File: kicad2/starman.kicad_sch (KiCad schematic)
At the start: 183 parts, among them J1 Conn_01x12, J2 Conn_01x10, J3 Conn_01x12, U1 ESP32-S2-MINI-1, U2 PCA9959, U3 PCA9959, U4 PCA9959, U5 PCA9959, U6 PCA9959, U7 PCA9959, U8 MIC29310-5.0WU, U9 LF33_TO220, Y1 20Mhz, Y2 20Mhz, Y3 20Mhz, Y4 20Mhz, Y5 20Mhz, Y6 20Mhz

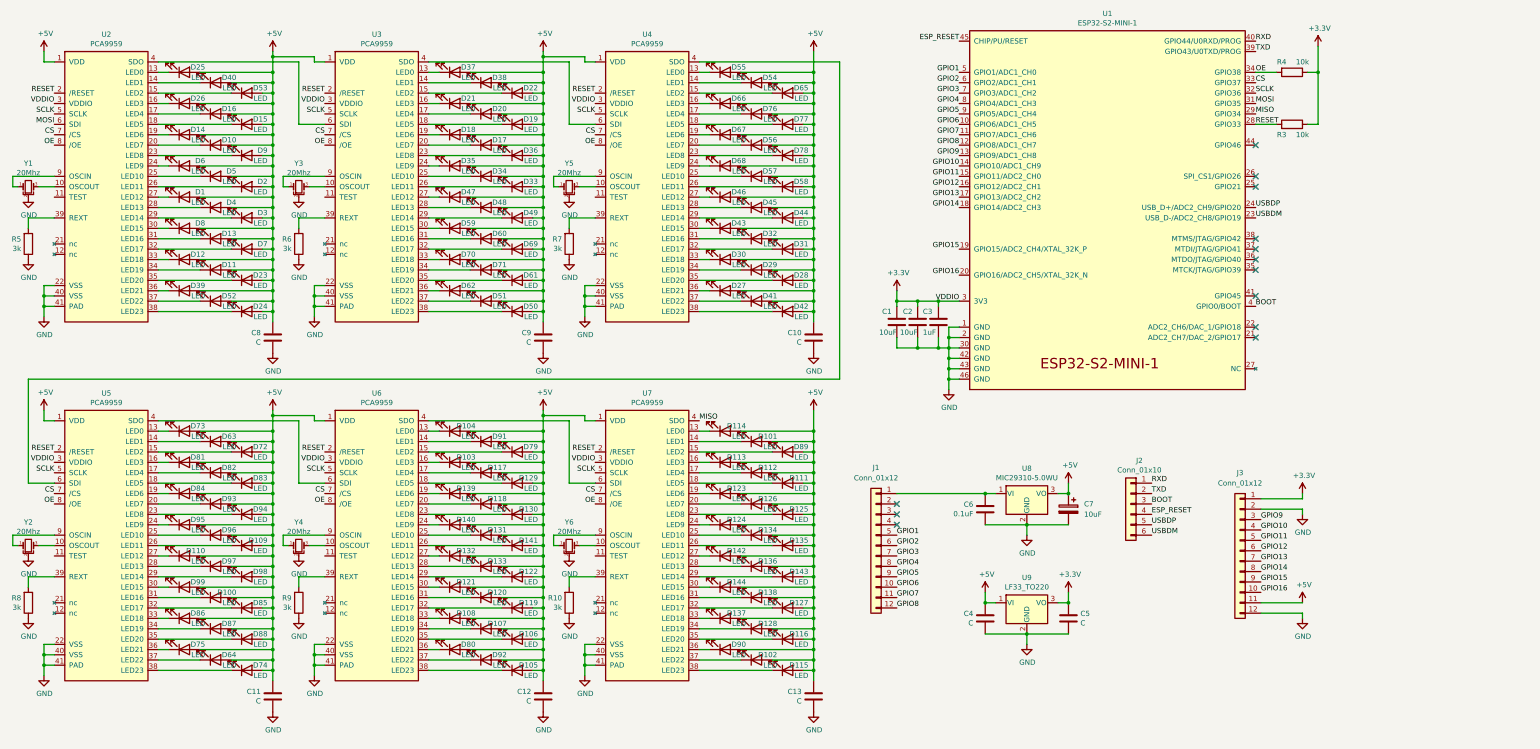
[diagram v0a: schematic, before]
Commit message: Complete routing of all GPIO pins
Also fixed paths to 3d components
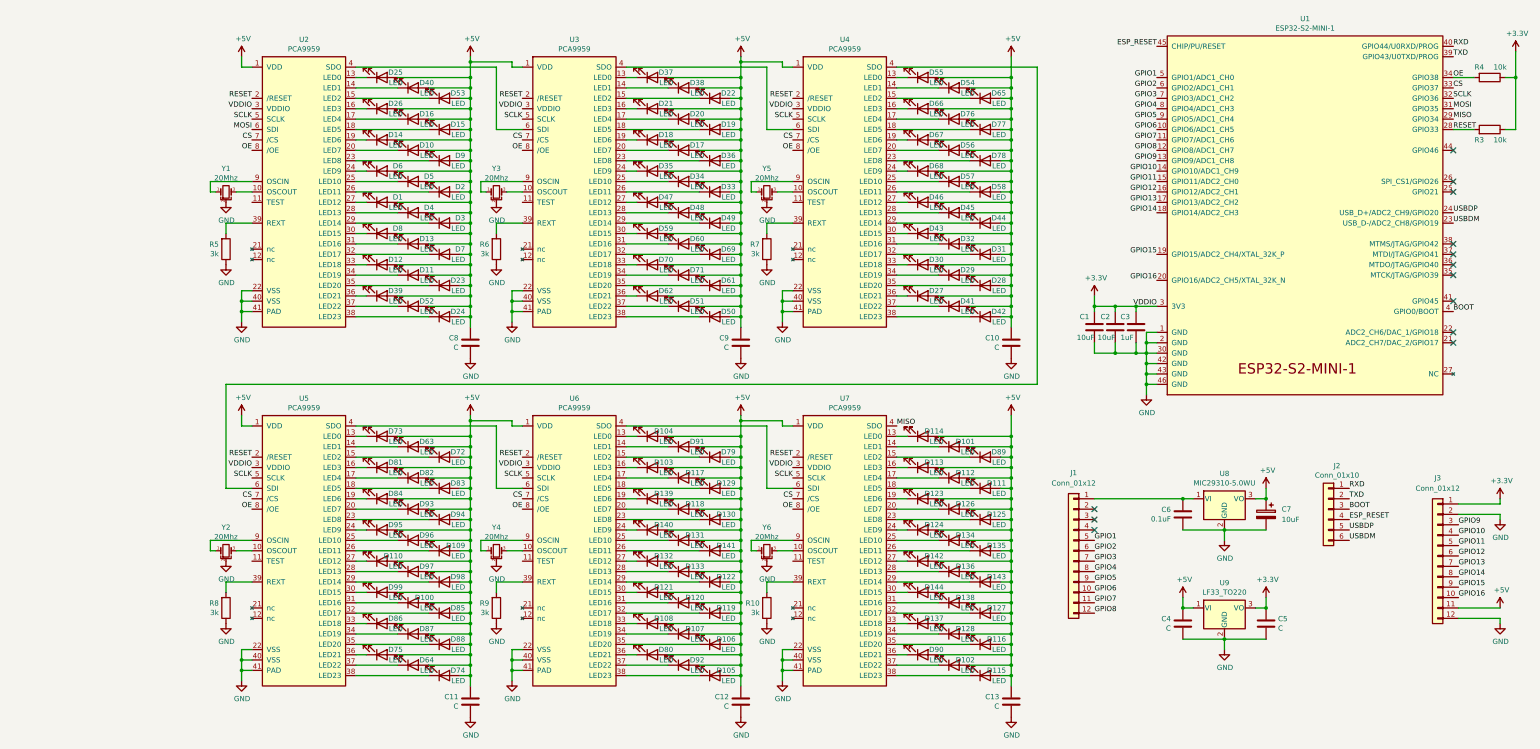
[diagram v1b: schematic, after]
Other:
- moved on the sheet: C1, C10, C11, C12, C13, C2, C3, C4, C5, C6, C7, C8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

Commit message: Added daughter board for power and buttons
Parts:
- added C14: 0.1uF, Capacitor_SMD:C_0805_2012Metric, symbol Device:C
- added C15: (no value), Capacitor_SMD:C_0805_2012Metric, symbol Device:C
- added J10: Barrel_Jack_MountingPin, Connector_BarrelJack:BarrelJack_CUI_PJ-063AH_Horizontal, symbol Connector:Barrel_Jack_MountingPin
- added J11: USB_B_Micro, Connector_USB:USB_Micro-B_Molex-105133-0031, symbol Connector:USB_B_Micro
- added J4: Conn_01x10, Connector_PinHeader_2.54mm:PinHeader_1x06_P2.54mm_Vertical, symbol Connector_Generic:Conn_01x06
- added J5: Conn_02x03_Counter_Clockwise, Connector_PinHeader_2.54mm:PinHeader_2x03_P2.54mm_Vertical, symbol Connector_Generic:Conn_02x03_Counter_Clockwise
- added J6, J8: Conn_01x12, Connector_PinHeader_2.54mm:PinHeader_1x12_P2.54mm_Vertical, symbol Connector_Generic:Conn_01x12
- added J7: Conn_01x10, Connector_PinHeader_2.54mm:PinHeader_1x10_P2.54mm_Vertical, symbol Connector_Generic:Conn_01x10
- added J9: Conn_01x08, Connector_PinHeader_2.54mm:PinHeader_1x10_P2.54mm_Vertical, symbol Connector_Generic:Conn_01x10
- added R1, R3: 10k, Resistor_SMD:R_0805_2012Metric, symbol Device:R
- added R2: (no value), Resistor_SMD:R_0805_2012Metric, symbol Device:R
- added SW1, SW2: (no value), symbol Switch:SW_SPST
- added SW3: SW_SPST, Button_Switch_SMD:SW_SPST_PTS810, symbol Switch:SW_SPST
- renumbered R4 to R11, R3 to R12
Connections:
- net BOOT renamed GPIO0
- net ESP_RESET renamed EN
- new net +3.3VA: J7.1 (Pin_1), J8.1 (Pin_1), R1.2, R2.2, R3.2
- new net +5VA: J8.11 (Pin_11), J9.1 (Pin_1)
- new net GNDA: C14.1, C15.1, J10.2, J10.MP (MountPin), J11.5 (GND), J11.6 (Shield), J5.2 (Pin_2), J7.10 (Pin_10), J8.12 (Pin_12), J8.2 (Pin_2), J9.10 (Pin_10), SW1.2 (B), SW2.2 (B), SW3.2 (B)
- new net VCC: J10.1, J6.1 (Pin_1)
- new net ext_EN: C14.2, C15.2, J4.4 (Pin_4), J5.4 (Pin_4), R2.1, SW2.1 (A)
- new net ext_GPIO0: J4.3 (Pin_3), J5.1 (Pin_1), R1.1, SW1.1 (A)
- new net ext_GPIO1: J6.5 (Pin_5), J7.2 (Pin_2), R3.1, SW3.1 (A)
- new net ext_GPIO10: J8.4 (Pin_4), J9.3 (Pin_3)
- new net ext_GPIO11: J8.5 (Pin_5), J9.4 (Pin_4)
- new net ext_GPIO12: J8.6 (Pin_6), J9.5 (Pin_5)
- new net ext_GPIO13: J8.7 (Pin_7), J9.6 (Pin_6)
- new net ext_GPIO14: J8.8 (Pin_8), J9.7 (Pin_7)
- new net ext_GPIO15: J8.9 (Pin_9), J9.8 (Pin_8)
- new net ext_GPIO16: J8.10 (Pin_10), J9.9 (Pin_9)
- new net ext_GPIO2: J6.6 (Pin_6), J7.3 (Pin_3)
- new net ext_GPIO3: J6.7 (Pin_7), J7.4 (Pin_4)
- new net ext_GPIO4: J6.8 (Pin_8), J7.5 (Pin_5)
- new net ext_GPIO5: J6.9 (Pin_9), J7.6 (Pin_6)
- new net ext_GPIO6: J6.10 (Pin_10), J7.7 (Pin_7)
- new net ext_GPIO7: J6.11 (Pin_11), J7.8 (Pin_8)
- new net ext_GPIO8: J6.12 (Pin_12), J7.9 (Pin_9)
- new net ext_GPIO9: J8.3 (Pin_3), J9.2 (Pin_2)
- new net ext_RXD: J4.1 (Pin_1), J5.6 (Pin_6)
- new net ext_TXD: J4.2 (Pin_2), J5.5 (Pin_5)
- new net ext_USBDM: J11.2 (D-), J4.6 (Pin_6)
- new net ext_USBDP: J11.3 (D+), J4.5 (Pin_5)
- no-connect marks 13 -> 19

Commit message: Added sound resistors, channels, volume, and speaker
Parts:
- removed J11: USB_B_Micro, Connector_USB:USB_Micro-B_Molex-105133-0031, symbol Connector:USB_B_Micro
- removed R1: 10k, Resistor_SMD:R_0805_2012Metric, symbol Device:R
- removed SW1: (no value), symbol Switch:SW_SPST
- added LS1: (no value), symbol Device:Speaker
- added R4, R5, R6: 75, Resistor_SMD:R_0805_2012Metric, symbol Device:R
- added R7: (no value), Resistor_SMD:R_0805_2012Metric, symbol Device:R
- added RV1: (no value), symbol Device:R_Potentiometer
- C15: value (none) -> 1uF
- J4: value Conn_01x10 -> (none); footprint Connector_PinHeader_2.54mm:PinHeader_1x06_P2.54mm_Vertical -> (none)
- R2: value (none) -> 10k
- SW1: renamed from SW2; value (none) -> SW_SPST; footprint (none) -> Button_Switch_SMD:SW_SPST_PTS810
- renumbered R7 to R10, R8 to R11, R9 to R12, R10 to R13, R11 to R14, R12 to R15, R5 to R8, R6 to R9, SW3 to SW2
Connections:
- net ext_USBDM is gone; now on net GNDA: J4.6 (Pin_6)
- net GND: now also J2.6 (Pin_6)
- net GNDA: now also LS1.2
- net at U1.21 (ADC2_CH7/DAC_2/GPIO17): now also R4.2
- net at U1.22 (ADC2_CH6/DAC_1/GPIO18): now also R5.2
- net USBDM: no longer names the net of U1.23 (USB_D-/ADC2_CH8/GPIO19)
- net USBDM: now also R6.2; no longer J2.6 (Pin_6)
- net USBDP: no longer names the net of U1.24 (USB_D+/ADC2_CH9/GPIO20)
- net USBDP: now also R7.2; no longer J2.5 (Pin_5)
- net ext_USBDP renamed ext_SOUND
- net ext_SOUND: now also RV1.1
- new net: LS1.1, RV1.3
- new net SOUND: J2.5 (Pin_5), R4.1, R5.1, R6.1, R7.1
- no-connect marks 19 -> 16
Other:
- moved on the sheet: C14, C15, J10, J4, J5, R2, R3, SW1, SW2

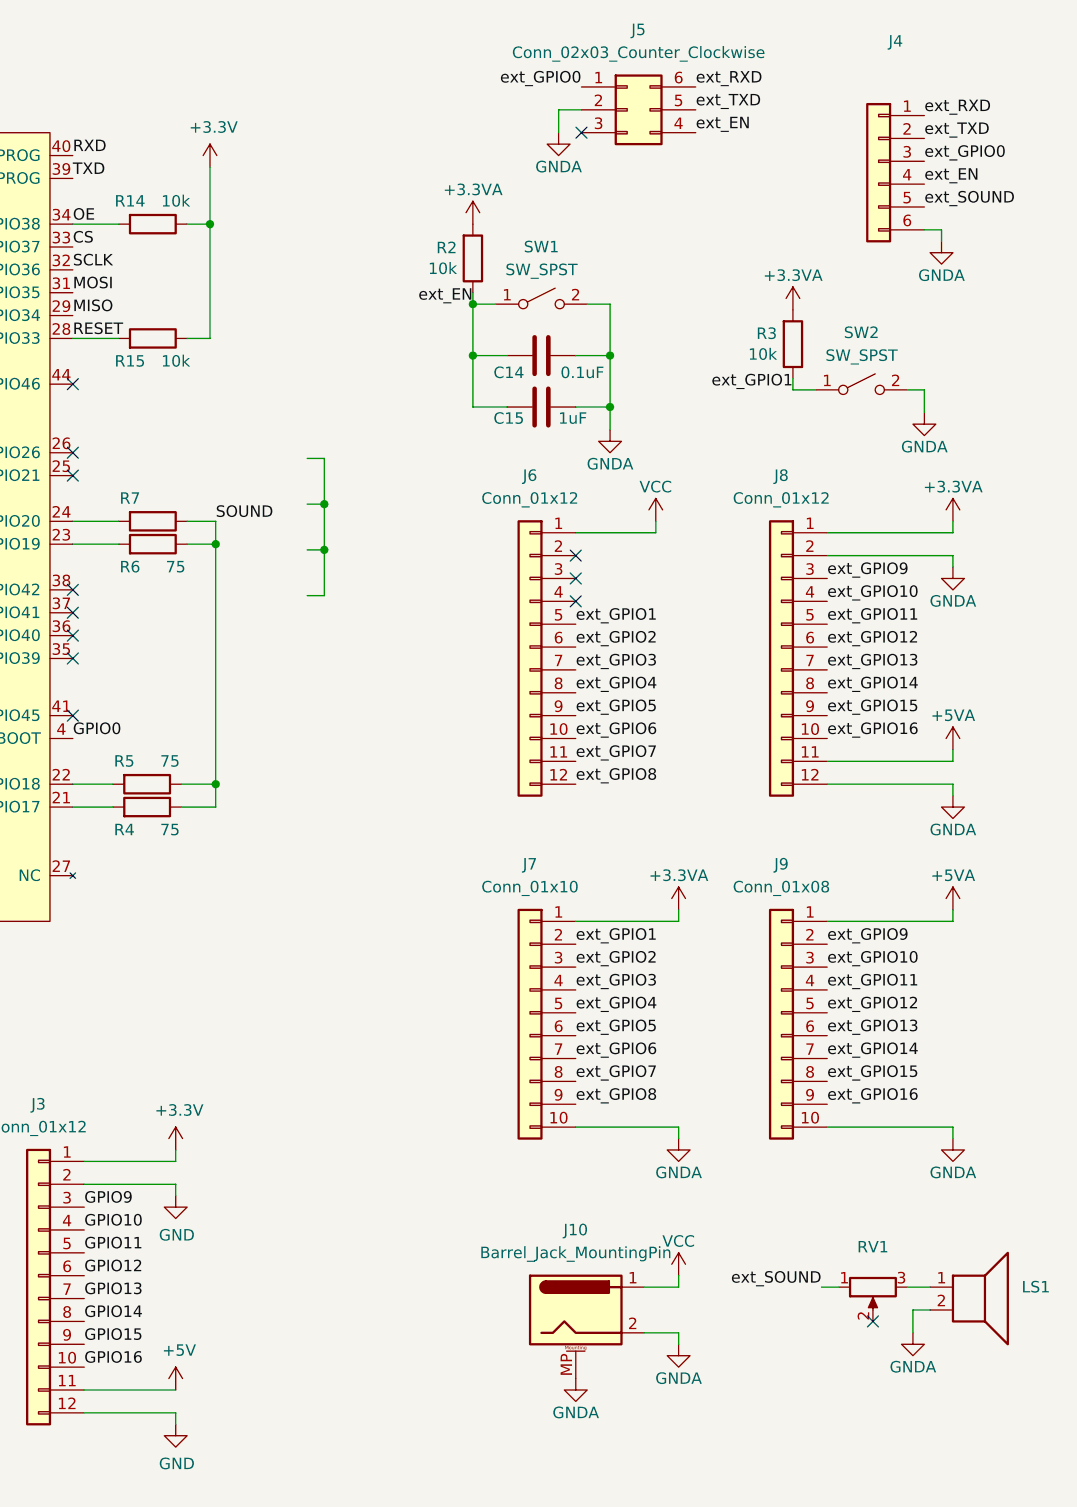
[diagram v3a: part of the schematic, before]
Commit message: Fixed DRC errors
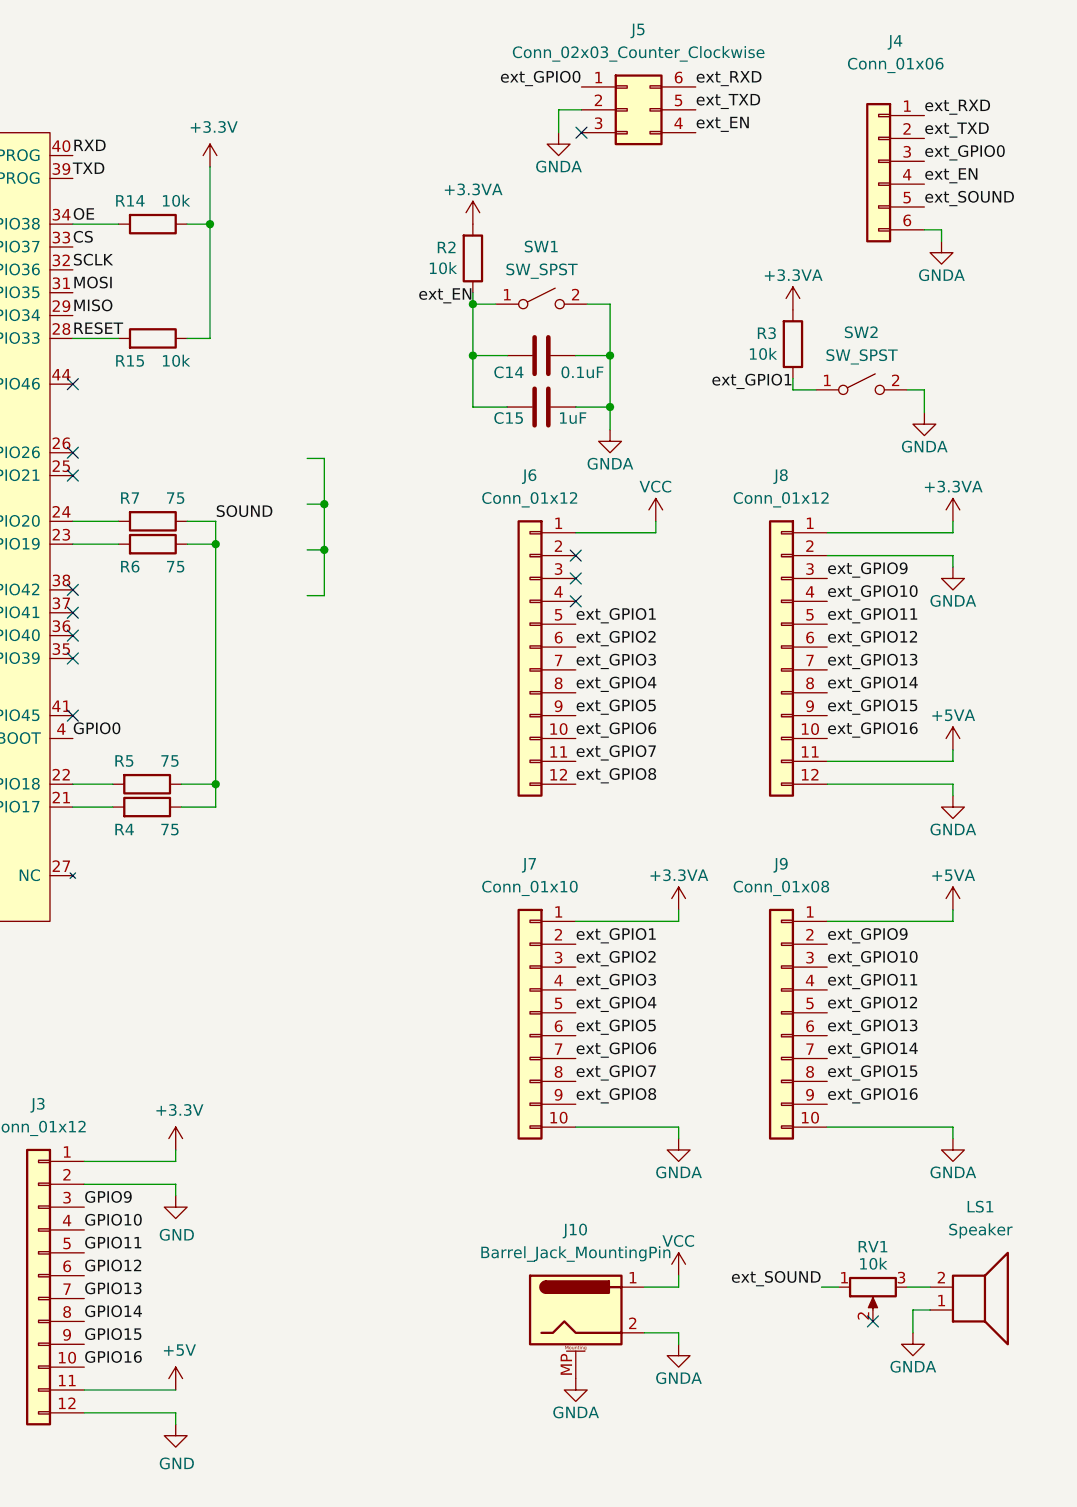
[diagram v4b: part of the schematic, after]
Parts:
- J4: value (none) -> Conn_01x06; footprint (none) -> Connector_PinHeader_2.54mm:PinHeader_1x06_P2.54mm_Vertical
- LS1: value (none) -> Speaker; footprint (none) -> Buzzer_Beeper:MagneticBuzzer_StarMicronics_HMB-06_HMB-12
- R7: value (none) -> 75
- RV1: value (none) -> 10k; footprint (none) -> Potentiometer_SMD:Potentiometer_ACP_CA9-VSMD_Vertical
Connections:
- net GNDA: now also LS1.1; no longer LS1.2
- net at RV1.3: now also LS1.2; no longer LS1.1
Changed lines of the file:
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@@
     (in_bom yes) (on_board yes)
     (property "Reference" "J4" (id 0) (at 410.21 10.16 0))
-    (property "Value" "" (id 1) (at 410.21 12.7 0))
-    (property "Footprint" "" (id 2) (at 408.305 23.495 0)
+    (property "Value" "Conn_01x06" (id 1) (at 410.21 12.7 0))
+    (property "Footprint" "Connector_PinHeader_2.54mm:PinHeader_1x06_P2.54mm_Vertical" (id 2) (at 408.305 23.495 0)
       (effects (font (size 1.27 1.27)) hide)
     )
@@
     (pin "1")
   )
-  (symbol (lib_id "Device:Speaker") (at 419.1 148.59 0) (unit 1)
+  (symbol (lib_id "Device:Speaker") (at 419.1 151.13 0) (mirror x) (unit 1)
     (in_bom yes) (on_board yes) (fields_autoplaced)
-    (property "Reference" "LS1" (id 0) (at 424.18 148.5899 0)
-      (effects (font (size 1.27 1.27)) (justify left))
-    )
-    (property "Value" "" (id 1) (at 424.18 151.1299 0)
-      (effects (font (size 1.27 1.27)) (justify left))
-    )
-    (property "Footprint" "" (id 2) (at 419.1 153.67 0)
+    (property "Reference" "LS1" (id 0) (at 419.608 139.7 0))
+    (property "Value" "Speaker" (id 1) (at 419.608 142.24 0))
+    (property "Footprint" "Buzzer_Beeper:MagneticBuzzer_StarMicronics_HMB-06_HMB-12" (id 2) (at 419.1 146.05 0)
       (effects (font (size 1.27 1.27)) hide)
     )
@@
     (in_bom yes) (on_board yes)
     (property "Reference" "RV1" (id 0) (at 407.67 144.145 90))
-    (property "Value" "" (id 1) (at 407.67 146.05 90))
-    (property "Footprint" "" (id 2) (at 407.67 148.59 0)
+    (property "Value" "10k" (id 1) (at 407.67 146.05 90))
+    (property "Footprint" "Potentiometer_SMD:Potentiometer_ACP_CA9-VSMD_Vertical" (id 2) (at 407.67 148.59 0)
       (effects (font (size 1.27 1.27)) hide)
     )
@@
     (in_bom yes) (on_board yes)
     (property "Reference" "R7" (id 0) (at 325.12 60.96 90))
-    (property "Value" "" (id 1) (at 330.2 60.96 90))
+    (property "Value" "75" (id 1) (at 330.2 60.96 90))
     (property "Footprint" "Resistor_SMD:R_0805_2012Metric" (id 2) (at 327.66 61.722 90)
       (effects (font (size 1.27 1.27)) hide)

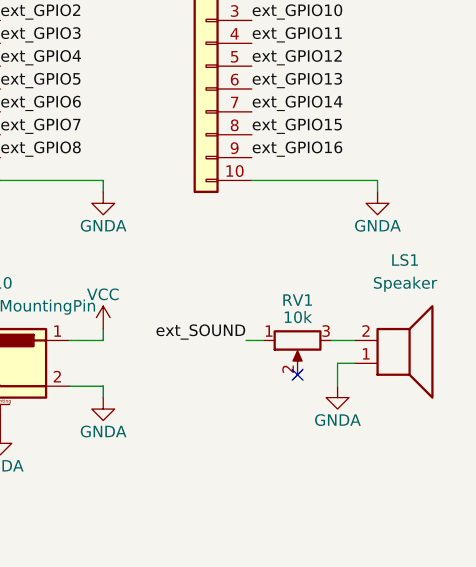
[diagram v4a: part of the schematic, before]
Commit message: Added dimensions and a label
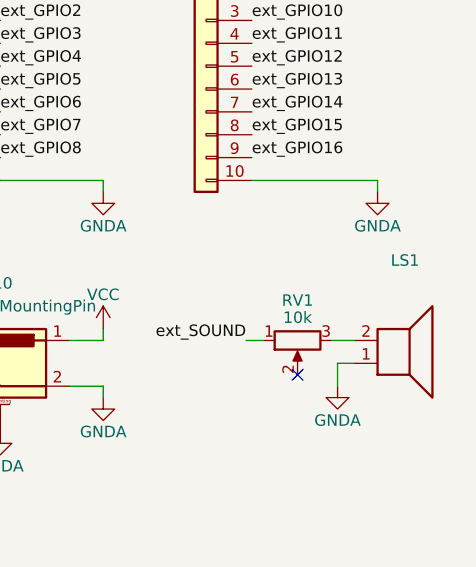
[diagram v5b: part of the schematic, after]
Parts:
- LS1: value Speaker -> (none); footprint Buzzer_Beeper:MagneticBuzzer_StarMicronics_HMB-06_HMB-12 -> (none)
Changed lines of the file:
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@@
     (in_bom yes) (on_board yes) (fields_autoplaced)
     (property "Reference" "LS1" (id 0) (at 419.608 139.7 0))
-    (property "Value" "Speaker" (id 1) (at 419.608 142.24 0))
-    (property "Footprint" "Buzzer_Beeper:MagneticBuzzer_StarMicronics_HMB-06_HMB-12" (id 2) (at 419.1 146.05 0)
+    (property "Value" "" (id 1) (at 419.608 142.24 0))
+    (property "Footprint" "" (id 2) (at 419.1 146.05 0)
       (effects (font (size 1.27 1.27)) hide)
     )
